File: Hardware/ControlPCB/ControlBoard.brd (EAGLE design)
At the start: 100 x 47.5 mm, 14 parts, among them IC1 TPS774

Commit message: Some PCB changes
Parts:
- added R7: 36k, resistor:M2012
- added S2: DTSM-6, switch-tact:DTSM-6
- R4, R5: value (none) -> 0
- S1: device SparkFun-Electromechanical:TACTILE_SWITCH_SMD-2 -> switch-tact:DTSM-6
- moved S1 4.49 mm to (12.1, 18.4), turned to 90 degrees
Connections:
- net !RST: now also S2.1, S2.2
- net GND: now also R7.2, S1.1, S2.3, S2.4; no longer X2.4
- net GPIO0: now also S1.3, S1.4; no longer S1.1
- net OE: now also R7.1
- net VCC: now also X2.4
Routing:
- net GPIO0: track 66.3 -> 54.1 mm
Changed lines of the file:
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@@
 <setting verticaltext="up"/>
 </settings>
-<grid distance="25" unitdist="mil" unit="mm" style="lines" multiple="1" display="no" altdistance="5" altunitdist="mil" altunit="mil"/>
+<grid distance="0.05" unitdist="inch" unit="inch" style="lines" multiple="1" display="yes" altdistance="0.025" altunitdist="inch" altunit="inch"/>
 <layers>
 <layer number="1" name="Top" color="4" fill="1" visible="yes" active="yes"/>
@@
 <layer number="106" name="bPlate" color="7" fill="1" visible="yes" active="yes"/>
 <layer number="107" name="Crop" color="7" fill="1" visible="yes" active="yes"/>
+<layer number="108" name="tplace-old" color="10" fill="1" visible="yes" active="yes"/>
+<layer number="109" name="ref-old" color="11" fill="1" visible="yes" active="yes"/>
+<layer number="116" name="Patch_BOT" color="9" fill="4" visible="yes" active="yes"/>
+<layer number="121" name="_tsilk" color="7" fill="1" visible="yes" active="yes"/>
+<layer number="122" name="_bsilk" color="7" fill="1" visible="yes" active="yes"/>
+<layer number="125" name="_tNames" color="7" fill="1" visible="yes" active="yes"/>
 <layer number="144" name="Drill_legend" color="7" fill="1" visible="yes" active="yes"/>
 <layer number="150" name="Notes" color="7" fill="1" visible="yes" active="yes"/>
@@
 <layer number="155" name="FabDoc3" color="7" fill="1" visible="yes" active="yes"/>
 <layer number="199" name="Contour" color="7" fill="1" visible="yes" active="yes"/>
+<layer number="200" name="200bmp" color="1" fill="10" visible="yes" active="yes"/>
+<layer number="201" name="201bmp" color="2" fill="10" visible="yes" active="yes"/>
+<layer number="202" name="202bmp" color="3" fill="10" visible="yes" active="yes"/>
+<layer number="203" name="203bmp" color="4" fill="10" visible="yes" active="yes"/>
+<layer number="204" name="204bmp" color="5" fill="10" visible="yes" active="yes"/>
+<layer number="205" name="205bmp" color="6" fill="10" visible="yes" active="yes"/>
+<layer number="206" name="206bmp" color="7" fill="10" visible="yes" active="yes"/>
+<layer number="207" name="207bmp" color="8" fill="10" visible="yes" active="yes"/>
+<layer number="208" name="208bmp" color="9" fill="10" visible="yes" active="yes"/>
+<layer number="209" name="209bmp" color="7" fill="1" visible="yes" active="yes"/>
+<layer number="210" name="210bmp" color="7" fill="1" visible="yes" active="yes"/>
+<layer number="211" name="211bmp" color="7" fill="1" visible="yes" active="yes"/>
+<layer number="212" name="212bmp" color="7" fill="1" visible="yes" active="yes"/>
+<layer number="213" name="213bmp" color="7" fill="1" visible="yes" active="yes"/>
+<layer number="214" name="214bmp" color="7" fill="1" visible="yes" active="yes"/>
+<layer number="215" name="215bmp" color="7" fill="1" visible="yes" active="yes"/>
+<layer number="216" name="216bmp" color="7" fill="1" visible="yes" active="yes"/>
 <layer number="217" name="217bmp" color="18" fill="1" visible="no" active="no"/>
 <layer number="218" name="218bmp" color="19" fill="1" visible="no" active="no"/>
@@
 <element name="R2" library="resistor" package="R1206" value="4.7K" x="24.13" y="15.24" rot="R90"/>
 <element name="R3" library="resistor" package="R1206" value="4.7K" x="20.32" y="15.24" rot="R90"/>
-<element name="S1" library="SparkFun-Electromechanical" package="TACTILE_SWITCH_SMD-2" value="FlashSW" x="7.62" y="19.05"/>
+<element name="S1" library="switch-tact" package="DTSM-6" value="FlashSW" x="12.065" y="18.415" rot="R90"/>
 <element name="U1" library="esp8266modules" package="ESP12E-SMD" value="" x="40.64" y="23.495" rot="R90"/>
 <element name="C3" library="SparkFun-Capacitors" package="EIA3528" value="10uF" x="22.225" y="6.985" rot="R90">
@@
 <element name="X1" library="con-amp" package="SMDTOP20" value="" x="78.105" y="27.305" rot="R270"/>
 <element name="X2" library="con-amp" package="SMDTOP4" value="" x="7.62" y="27.305" rot="R270"/>
-<element name="R4" library="resistor" package="R5025W" value="" x="60.9854" y="35.6108" rot="R270"/>
-<element name="R5" library="resistor" package="R5025W" value="" x="24.13" y="29.21" rot="R90"/>
+<element name="R4" library="resistor" package="R5025W" value="0" x="60.9854" y="35.6108" rot="R270"/>
+<element name="R5" library="resistor" package="R5025W" value="0" x="24.13" y="29.21" rot="R90"/>
 <element name="R6" library="SparkFun-Passives" package="SJ_2S-TRACE" value="" x="67.945" y="35.56"/>
 <element name="SJ1" library="SparkFun-Passives" package="SJ_2S-TRACE" value="" x="34.925" y="35.56" rot="R90"/>
+<element name="R7" library="resistor" package="M2012" value="36k" x="66.675" y="27.94" rot="R180"/>
+<element name="S2" library="switch-tact" package="DTSM-6" value="DTSM-6" x="5.08" y="17.78" rot="R270"/>
 </elements>
 <signals>
@@
 <vertex x="0" y="33.02"/>
 </polygon>
-<contactref element="S1" pad="2"/>
+<contactref element="S1" pad="1"/>
 <contactref element="C3" pad="C"/>
 <contactref element="X1" pad="7"/>
@@
 <contactref element="X1" pad="19"/>
 <contactref element="X2" pad="2"/>
-<contactref element="X2" pad="4"/>
 <via x="4" y="7.5" extent="1-16" drill="3.2" diameter="3.81"/>
 <via x="96" y="7.5" extent="1-16" drill="3.2" diameter="3.81"/>
-<wire x1="59.055" y1="27.153" x2="80.645" y2="26.67" width="0" layer="19" extent="1-1"/>
+<contactref element="R7" pad="2"/>
+<contactref element="S1" pad="2"/>
+<contactref element="S2" pad="3"/>
+<contactref element="S2" pad="4"/>
+<wire x1="65.725" y1="27.94" x2="80.645" y2="26.67" width="0" layer="19" extent="1-1"/>
 </signal>
 <signal name="RB_C" class="2">
@@
 <wire x1="40.84" y1="35.125" x2="45.085" y2="39.37" width="0.6096" layer="1"/>
 <wire x1="45.085" y1="39.37" x2="46.99" y2="39.37" width="1.6764" layer="1"/>
-<wire x1="46.99" y1="39.37" x2="68.58" y2="27.94" width="0" layer="19" extent="1-1"/>
+<contactref element="R7" pad="1"/>
+<wire x1="67.625" y1="27.94" x2="68.58" y2="27.94" width="0" layer="19" extent="1-1"/>
+<wire x1="46.99" y1="39.37" x2="67.625" y2="27.94" width="0" layer="19" extent="1-1"/>
 </signal>
 <signal name="MOSI" class="2">
@@
 <contactref element="R3" pad="2"/>
 <contactref element="U1" pad="GPIO0"/>
-<contactref element="S1" pad="1"/>
+<contactref element="S1" pad="3"/>
 <wire x1="42.84" y1="31.595" x2="42.84" y2="26.33" width="0.508" layer="1"/>
 <wire x1="42.84" y1="26.33" x2="37.465" y2="20.955" width="0.508" layer="1"/>
@@
 <wire x1="28.575" y1="19.685" x2="23.365" y2="19.685" width="0.508" layer="1"/>
 <wire x1="23.365" y1="19.685" x2="20.32" y2="16.662" width="0.508" layer="1"/>
-<wire x1="20.32" y1="16.662" x2="16.16" y2="20.8" width="0.508" layer="1"/>
-<wire x1="16.16" y1="20.8" x2="9.845" y2="20.8" width="0.508" layer="1"/>
 <contactref element="R4" pad="1"/>
 <wire x1="42.84" y1="31.595" x2="42.84" y2="33.95" width="0.508" layer="1"/>
@@
 <wire x1="48.895" y1="38.1" x2="60.8072" y2="38.1" width="0.508" layer="1"/>
 <wire x1="60.8072" y1="38.1" x2="60.9854" y2="37.9218" width="0.508" layer="1"/>
+<contactref element="S1" pad="4"/>
+<wire x1="14.315" y1="14.44" x2="20.32" y2="16.662" width="0" layer="19" extent="1-1"/>
+<wire x1="14.315" y1="22.39" x2="14.315" y2="14.44" width="0" layer="19" extent="1-1"/>
 </signal>
 <signal name="RXD" class="2">
@@
 <wire x1="48.895" y1="14.605" x2="48.895" y2="15.14" width="0.508" layer="1"/>
 <wire x1="48.895" y1="15.14" x2="48.84" y2="15.195" width="0.508" layer="1"/>
+<contactref element="X2" pad="4"/>
+<wire x1="20.32" y1="13.818" x2="5.08" y2="25.4" width="0" layer="19" extent="1-1"/>
 </signal>
 <signal name="!RST" class="2">
@@
 <wire x1="17.78" y1="15.24" x2="34.795" y2="15.24" width="0.508" layer="1"/>
 <wire x1="34.795" y1="15.24" x2="34.84" y2="15.195" width="0.508" layer="1"/>
+<contactref element="S2" pad="1"/>
+<contactref element="S2" pad="2"/>
+<wire x1="7.33" y1="13.805" x2="16.525" y2="13.985" width="0" layer="19" extent="1-1"/>
+<wire x1="7.33" y1="21.755" x2="7.33" y2="13.805" width="0" layer="19" extent="1-1"/>
 </signal>
 <signal name="N$6">

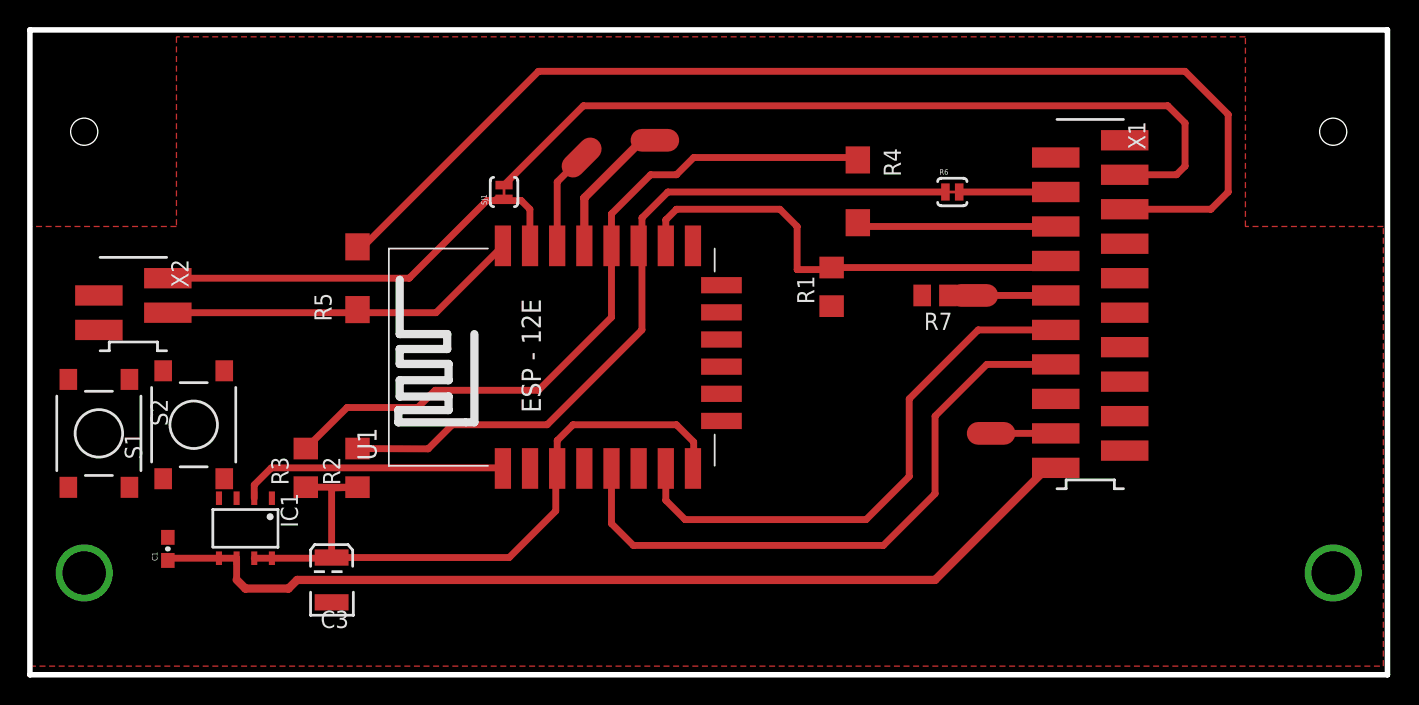
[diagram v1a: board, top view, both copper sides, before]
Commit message: Updated schematics and pcb
Cleaned up schematics and new board layout with milling code files.
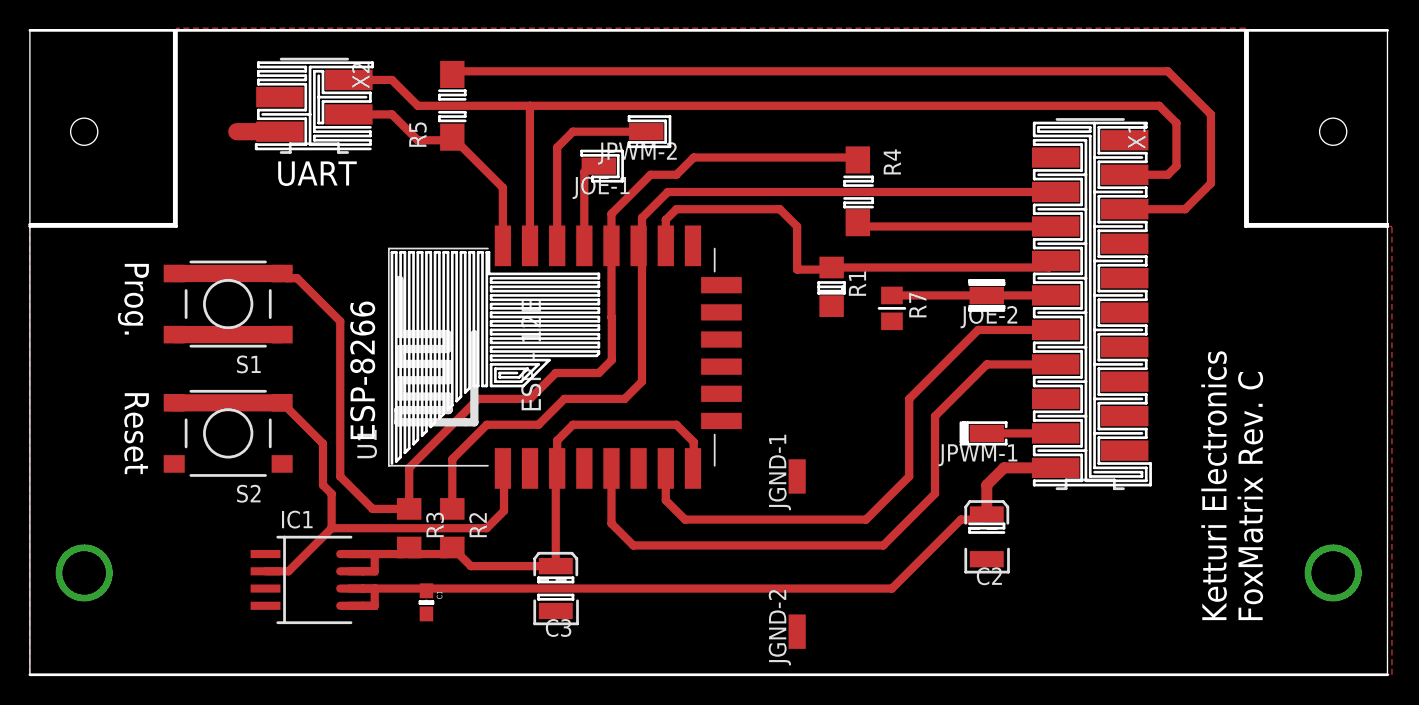
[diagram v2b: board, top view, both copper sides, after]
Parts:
- removed R6, SJ1: (no value), SparkFun-Passives:SJ_2S-TRACE
- added C2: 10uF, SparkFun-Capacitors:EIA3528
- added JGND-1, JGND-2, JOE-1, JOE-2, JPWM-1, JPWM-2: (no value), wirepad:SMD1,27-2,54
- IC1: value TPS774 -> TPS77333; device texas:DGK-R-PDSO-G8 -> texas:SOP-08
- S2: value DTSM-6 -> ResetSW
- X1: value (none) -> LedPanel
- X2: value (none) -> UART
- moved X2 19.8 mm to (21.0, 41.9)
- moved C1 19.5 mm to (29.2, 5.33), turned to 270 degrees
- moved C3 16.5 mm to (38.7, 6.35)
- moved R5 14.5 mm to (31.1, 41.9)
- moved S2 9.53 mm to (14.6, 17.8), turned to 180 degrees
- moved S1 9.25 mm to (14.6, 27.3), turned to 180 degrees
- moved R3 8.82 mm to (27.9, 10.8), turned to 270 degrees
- moved R2 8.28 mm to (31.1, 10.8), turned to 270 degrees
- moved IC1 6.35 mm to (21.0, 6.99), turned to 270 degrees
- moved R7 3.31 mm to (63.5, 27.0), turned to 270 degrees
- turned R1 to 270 degrees
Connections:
- removed net N$6: X1.2
- removed net RB_C: R6.2, X1.4
- removed net RB_D: SJ1.2, X1.3
- net !RST: now also S2.3, S2.4; no longer S2.1, S2.2
- net +5V: now also C2.A
- net CS: now also R1.1; no longer R1.2
- net GND: now also C2.C, JGND-1.1, JGND-2.1, R1.2, S2.1, S2.2; no longer R1.1, S2.3, S2.4
- net GPIO0: now also R3.1; no longer R3.2
- net GPIO2: now also R2.1, X1.4; no longer R2.2, R6.1
- net OE: now also JOE-1.1, JOE-2.1
- net PWM: now also JPWM-1.1, JPWM-2.1
- net RXD: now also X1.3; no longer SJ1.1
- net VCC: now also R2.2, R3.2; no longer R2.1, R3.1
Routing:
- net RB_D: track 61.0 -> 0.00 mm
- net RXD: track 32.7 -> 79.8 mm
- net GPIO0: track 54.1 -> 88.1 mm
- net !RST: track 19.8 -> 41.3 mm
- net RB_B: track 84.6 -> 69.5 mm
- net +5V: track 71.0 -> 61.6 mm
- net TXD: track 27.2 -> 18.1 mm
- net GND: track 0.00 -> 7.95 mm
- net GPIO2: track 56.3 -> 63.7 mm
- net RB_C: track 7.11 -> 0.00 mm
- net VCC: track 53.4 -> 47.3 mm
- net PWM: track 13.9 -> 19.4 mm
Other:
- outline, holes or cut-outs redrawn
- board text added: "ESP-8266"
- board text added: "Ketturi Electronics FoxMatrix Rev. C"
- board text added: "Prog."
- board text added: "Reset"
- board text added: "UART"
